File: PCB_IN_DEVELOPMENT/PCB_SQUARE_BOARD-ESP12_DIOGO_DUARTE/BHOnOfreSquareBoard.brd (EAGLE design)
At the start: 47.6 x 47.7 mm, 23 parts, among them J1 4p, J6 8p, J7 8p, K1 OMRON-G3MB-202P-SSR2, K2 OMRON-G3MB-202P-SSR2, Q1 S8050, Q2 S8050, U1 LM1117, U2 esp12

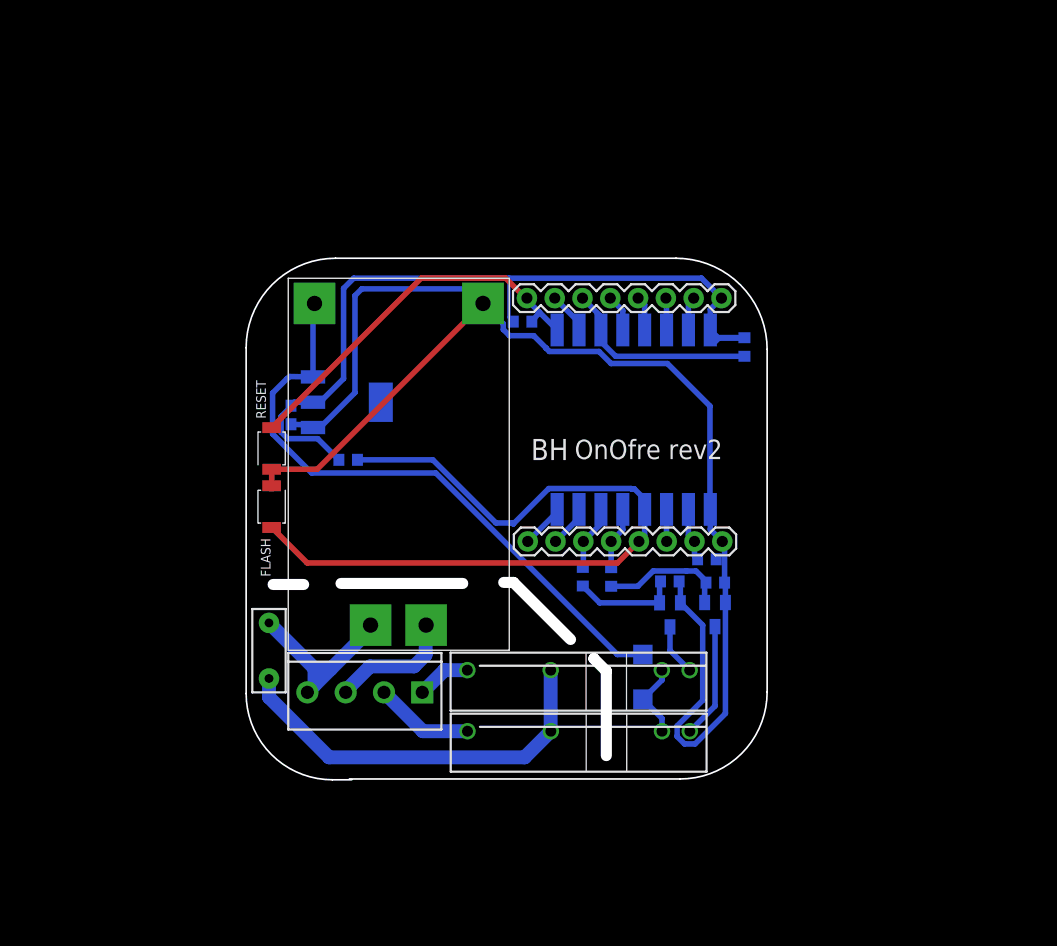
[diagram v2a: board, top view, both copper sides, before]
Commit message: Now with ground planes, like a pro! :)
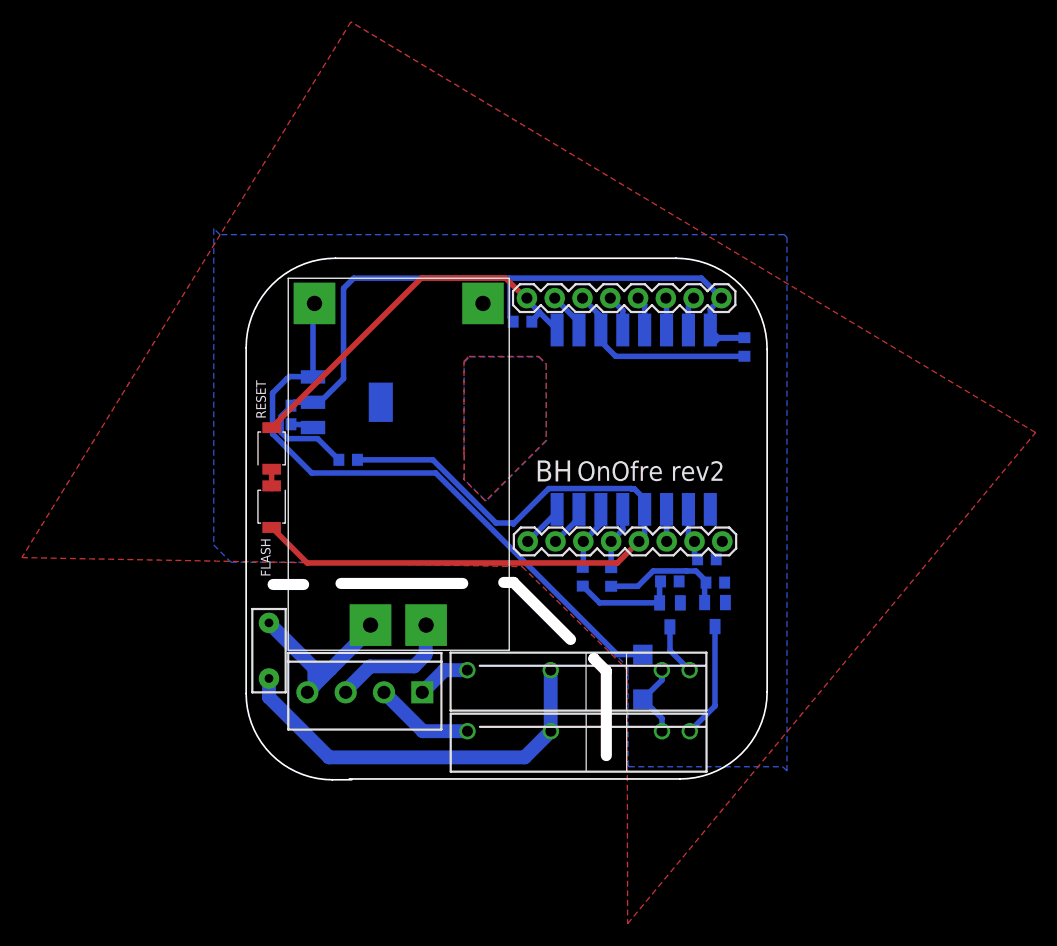
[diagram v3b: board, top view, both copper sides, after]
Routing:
- net GND: track 132.1 -> 3.88 mm
- added copper zone on layer 1, net ANT
- added copper zone on layer 16, net ANT2
- added copper zone on layer 1, net GND
- added copper zone on layer 16, net GND
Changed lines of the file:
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@@
 <board>
 <plain>
-<text x="29.4537375" y="31.077203125" size="1.9304" layer="25" font="vector" rot="R180">BH</text>
-<text x="43.5382625" y="31.013540625" size="1.778" layer="25" font="vector" rot="R180">OnOfre rev2</text>
+<text x="29.8455" y="29.118396875" size="1.9304" layer="25" font="vector" rot="R180">BH</text>
+<text x="43.762125" y="29.02675" size="1.778" layer="25" font="vector" rot="R180">OnOfre rev2</text>
 <wire x1="9.657421875" y1="-0.074365625" x2="7.882628125" y2="-0.074365625" width="0.1524" layer="20"/>
 <wire x1="7.882628125" y1="-0.074365625" x2="0" y2="7.8082625" width="0.1524" layer="20" curve="-90"/>
@@
 <contactref element="U1" pad="1"/>
 <contactref element="FLASH" pad="2"/>
-<wire x1="42.424275" y1="24.638371875" x2="42.424275" y2="22.806525" width="0.508" layer="16"/>
-<wire x1="42.424275" y1="22.806525" x2="43.5195875" y2="21.7112125" width="0.508" layer="16"/>
-<wire x1="43.806709375" y1="16.127984375" x2="43.806709375" y2="17.870971875" width="0.508" layer="16"/>
-<wire x1="43.806709375" y1="17.870971875" x2="43.730459375" y2="17.947221875" width="0.508" layer="16"/>
-<wire x1="43.730459375" y1="17.947221875" x2="43.730459375" y2="21.500340625" width="0.508" layer="16"/>
-<wire x1="43.730459375" y1="21.500340625" x2="43.5195875" y2="21.7112125" width="0.508" layer="16"/>
-<wire x1="39.689003125" y1="16.099009375" x2="39.689003125" y2="17.942521875" width="0.508" layer="16"/>
-<wire x1="39.689003125" y1="17.942521875" x2="39.573328125" y2="18.058196875" width="0.508" layer="16"/>
-<wire x1="43.015471875" y1="21.500340625" x2="43.730459375" y2="21.500340625" width="0.508" layer="16"/>
-<wire x1="39.689003125" y1="16.099009375" x2="41.7314875" y2="14.056525" width="0.508" layer="16"/>
-<wire x1="39.39009375" y1="4.8449625" x2="39.39009375" y2="3.88365" width="0.508" layer="16"/>
-<wire x1="39.39009375" y1="3.88365" x2="40.06984375" y2="3.2039" width="0.508" layer="16"/>
-<wire x1="40.06984375" y1="3.2039" x2="41.03115625" y2="3.2039" width="0.508" layer="16"/>
-<wire x1="41.7314875" y1="7.18635625" x2="39.39009375" y2="4.8449625" width="0.508" layer="16"/>
-<wire x1="41.03115625" y1="3.2039" x2="43.806709375" y2="5.979453125" width="0.508" layer="16"/>
-<wire x1="43.806709375" y1="5.979453125" x2="43.806709375" y2="16.127984375" width="0.508" layer="16"/>
-<wire x1="41.7314875" y1="14.056525" x2="41.7314875" y2="7.18635625" width="0.508" layer="16"/>
 <wire x1="6.11129375" y1="32.12116875" x2="6.11129375" y2="32.13063125" width="0.508" layer="16"/>
 <wire x1="4.100709375" y1="32.416790625" x2="5.30525" y2="32.374478125" width="0.508" layer="16"/>
 <wire x1="5.30525" y1="32.374478125" x2="6.11129375" y2="32.12116875" width="0.508" layer="16"/>
-<wire x1="6.11129375" y1="32.12116875" x2="6.75540625" y2="32.12116875" width="0.508" layer="16"/>
-<wire x1="10.563165625" y1="44.793384375" x2="20.60521875" y2="44.793384375" width="0.508" layer="16"/>
-<wire x1="20.60521875" y1="44.793384375" x2="21.648915625" y2="43.7496875" width="0.508" layer="16"/>
 <wire x1="21.648915625" y1="43.7496875" x2="21.648915625" y2="43.462690625" width="0.508" layer="16"/>
-<wire x1="6.75540625" y1="32.12116875" x2="9.947346875" y2="35.313109375" width="0.508" layer="16"/>
-<wire x1="9.947346875" y1="35.313109375" x2="9.947346875" y2="44.177565625" width="0.508" layer="16"/>
-<wire x1="9.947346875" y1="44.177565625" x2="10.563165625" y2="44.793384375" width="0.508" layer="16"/>
-<wire x1="38.504609375" y1="37.970928125" x2="42.39464375" y2="34.08089375" width="0.508" layer="16"/>
-<wire x1="42.39464375" y1="34.08089375" x2="42.39464375" y2="24.668003125" width="0.508" layer="16"/>
-<wire x1="42.39464375" y1="24.668003125" x2="42.424275" y2="24.638371875" width="0.508" layer="16"/>
 <wire x1="2.32974375" y1="26.78851875" x2="2.334090625" y2="26.792865625" width="1.016" layer="1" curve="90"/>
-<wire x1="21.648915625" y1="43.462690625" x2="23.50525" y2="41.60635625" width="0.508" layer="16"/>
-<wire x1="23.50525" y1="41.60635625" x2="23.50525" y2="41.07926875" width="0.508" layer="16"/>
-<wire x1="23.50525" y1="41.07926875" x2="24.070265625" y2="40.514253125" width="0.508" layer="16"/>
-<wire x1="24.070265625" y1="40.514253125" x2="26.28701875" y2="40.514253125" width="0.508" layer="16"/>
-<wire x1="26.28701875" y1="40.514253125" x2="27.417878125" y2="39.38339375" width="0.508" layer="16"/>
-<wire x1="27.417878125" y1="39.38339375" x2="27.417878125" y2="39.370034375" width="0.508" layer="16"/>
-<wire x1="27.417878125" y1="39.370034375" x2="27.714715625" y2="39.073196875" width="0.508" layer="16"/>
-<wire x1="27.714715625" y1="39.073196875" x2="32.25199375" y2="39.073196875" width="0.508" layer="16"/>
-<wire x1="32.25199375" y1="39.073196875" x2="33.3542625" y2="37.970928125" width="0.508" layer="16"/>
-<wire x1="33.3542625" y1="37.970928125" x2="38.504609375" y2="37.970928125" width="0.508" layer="16"/>
 <wire x1="2.32974375" y1="26.78851875" x2="2.334090625" y2="26.792865625" width="0.508" layer="1"/>
 <wire x1="2.334090625" y1="26.792865625" x2="2.334090625" y2="28.311728125" width="0.508" layer="1"/>
-<wire x1="2.334090625" y1="28.311728125" x2="6.497953125" y2="28.311728125" width="0.508" layer="1"/>
-<wire x1="6.497953125" y1="28.311728125" x2="21.648915625" y2="43.462690625" width="0.508" layer="1"/>
-<wire x1="43.015471875" y1="21.500340625" x2="42.964084375" y2="20.077509375" width="0" layer="19" extent="16-16"/>
+<polygon width="0.254" layer="1" rank="6">
+<vertex x="9.5792375" y="69.197496875"/>
+<vertex x="-20.49721875" y="20.230959375"/>
+<vertex x="25.2273" y="19.40715625"/>
+<vertex x="34.817715625" y="10.004121875"/>
+<vertex x="34.868159375" y="-13.232765625"/>
+<vertex x="72.1575375" y="31.662753125"/>
+</polygon>
+<polygon width="0.254" layer="16" rank="6">
+<vertex x="-2.958203125" y="50.279128125"/>
+<vertex x="-2.958203125" y="21.386634375"/>
+<vertex x="-1.38049375" y="19.808925"/>
+<vertex x="25.308990625" y="19.808925"/>
+<vertex x="25.374803125" y="19.7431125"/>
+<vertex x="34.9067875" y="10.211128125"/>
+<vertex x="34.9067875" y="9.608315625"/>
+<vertex x="34.9067875" y="1.1845125"/>
+<vertex x="34.972525" y="1.118775"/>
+<vertex x="49.039990625" y="1.118775"/>
+<vertex x="49.43485" y="0.723915625"/>
+<vertex x="49.43485" y="49.48969375"/>
+<vertex x="49.171896875" y="49.752646875"/>
+<vertex x="-2.401003125" y="49.752646875"/>
+<vertex x="-2.9610125" y="50.31265625"/>
+</polygon>
 </signal>
 <signal name="VCC">
@@
 <wire x1="3.7876" y1="31.10516875" x2="6.537203125" y2="31.10516875" width="0.508" layer="16"/>
 </signal>
+<signal name="ANT">
+<polygon width="0.254" layer="1" pour="cutout">
+<vertex x="19.9113375" y="29.804878125"/>
+<vertex x="19.9113375" y="38.175628125"/>
+<vertex x="20.355221875" y="38.6195125"/>
+<vertex x="26.759796875" y="38.6195125"/>
+<vertex x="27.42565" y="37.953659375"/>
+<vertex x="27.42565" y="30.946103125"/>
+<vertex x="21.877109375" y="25.3975625"/>
+<vertex x="19.923240625" y="27.35143125"/>
+<vertex x="19.923240625" y="29.793878125"/>
+<vertex x="19.914396875" y="29.802721875"/>
+<vertex x="19.90555625" y="29.802721875"/>
+<vertex x="19.8967125" y="29.793878125"/>
+<vertex x="19.9144" y="29.776190625"/>
+<vertex x="19.923240625" y="29.776190625"/>
+<vertex x="19.9144" y="29.76735"/>
+<vertex x="19.9144" y="29.767346875"/>
+<vertex x="19.90555625" y="29.776190625"/>
+<vertex x="19.90555625" y="29.785034375"/>
+<vertex x="19.90555625" y="29.793878125"/>
+<vertex x="19.90555625" y="29.802721875"/>
+<vertex x="19.9320875" y="29.776190625"/>
+<vertex x="19.940928125" y="29.776190625"/>
+</polygon>
+</signal>
+<signal name="ANT2">
+<polygon width="0.254" layer="16" pour="cutout">
+<vertex x="19.9224875" y="27.39834375"/>
+<vertex x="19.9224875" y="38.0723375"/>
+<vertex x="20.424484375" y="38.574334375"/>
+<vertex x="20.4509375" y="38.574334375"/>
+<vertex x="26.739465625" y="38.574334375"/>
+<vertex x="27.34714375" y="37.96665625"/>
+<vertex x="27.42645" y="37.96665625"/>
+<vertex x="27.42645" y="30.991571875"/>
+<vertex x="27.452871875" y="30.96515"/>
+<vertex x="27.452871875" y="30.91264375"/>
+<vertex x="21.983434375" y="25.44320625"/>
+<vertex x="21.877740625" y="25.44320625"/>
+<vertex x="21.798478125" y="25.52246875"/>
+<vertex x="19.949021875" y="27.371925"/>
+<vertex x="19.948909375" y="27.371925"/>
+<vertex x="19.932075" y="27.371925"/>
+<vertex x="19.90905" y="27.39495"/>
+<vertex x="19.90905" y="27.441140625"/>
+<vertex x="19.91615625" y="27.448246875"/>
+<vertex x="19.91615625" y="27.40205625"/>
+<vertex x="19.905496875" y="27.391396875"/>
+<vertex x="19.905496875" y="27.38784375"/>
+<vertex x="19.91615625" y="27.377184375"/>
+<vertex x="19.926815625" y="27.38784375"/>
+<vertex x="19.926815625" y="27.405609375"/>
+</polygon>
+</signal>
 </signals>
+<errors>
+</errors>
 </board>
 </drawing>
